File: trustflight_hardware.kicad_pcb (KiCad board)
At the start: 4 copper layers, 30.5 x 27 mm, 69 parts, among them J1 Conn_01x02, J10 Dronecode_Telemetry, J2 Conn_01x02, J3 Conn_01x02, J4 Conn_01x02, J5 Conn_01x01, J6 Conn_01x02, J7 Conn_01x02, J8 Conn_01x03, J9 swd-4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

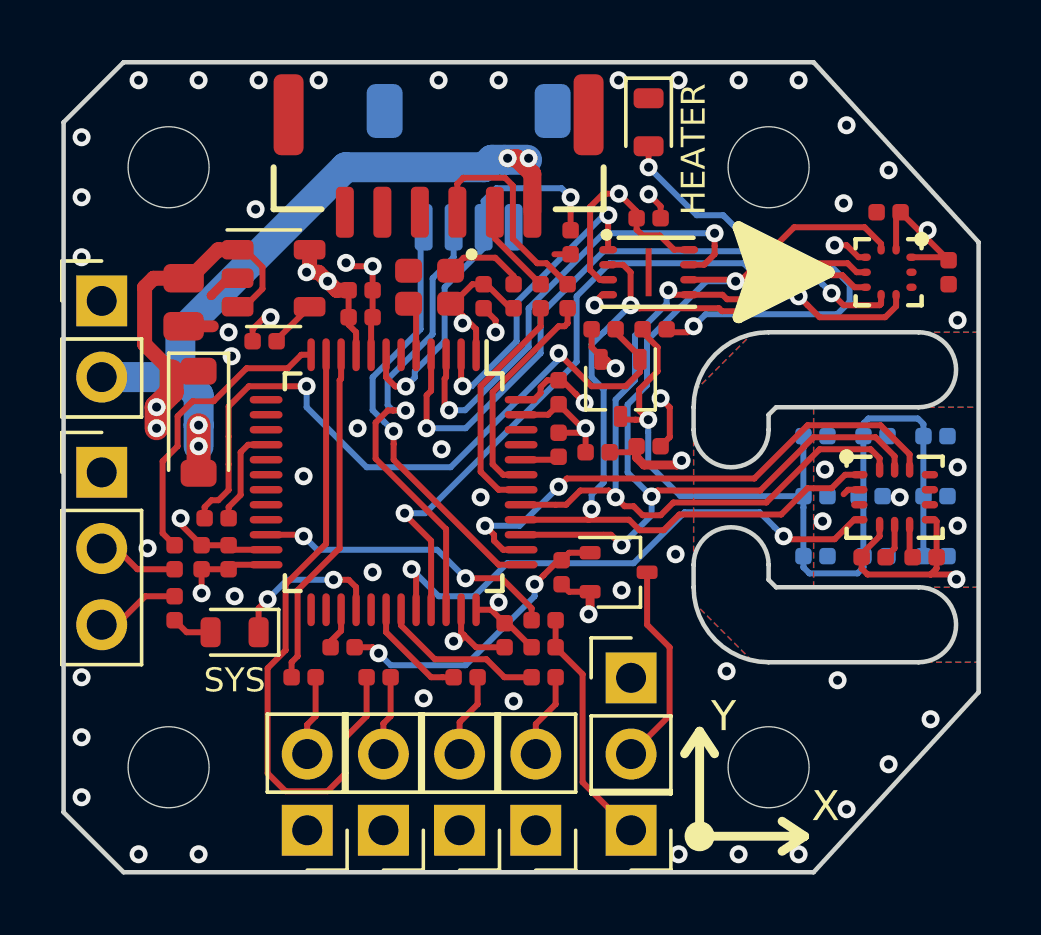
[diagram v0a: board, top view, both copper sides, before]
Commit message: Rev. B, fixed non 5V tolerant pins for heater/buzzer
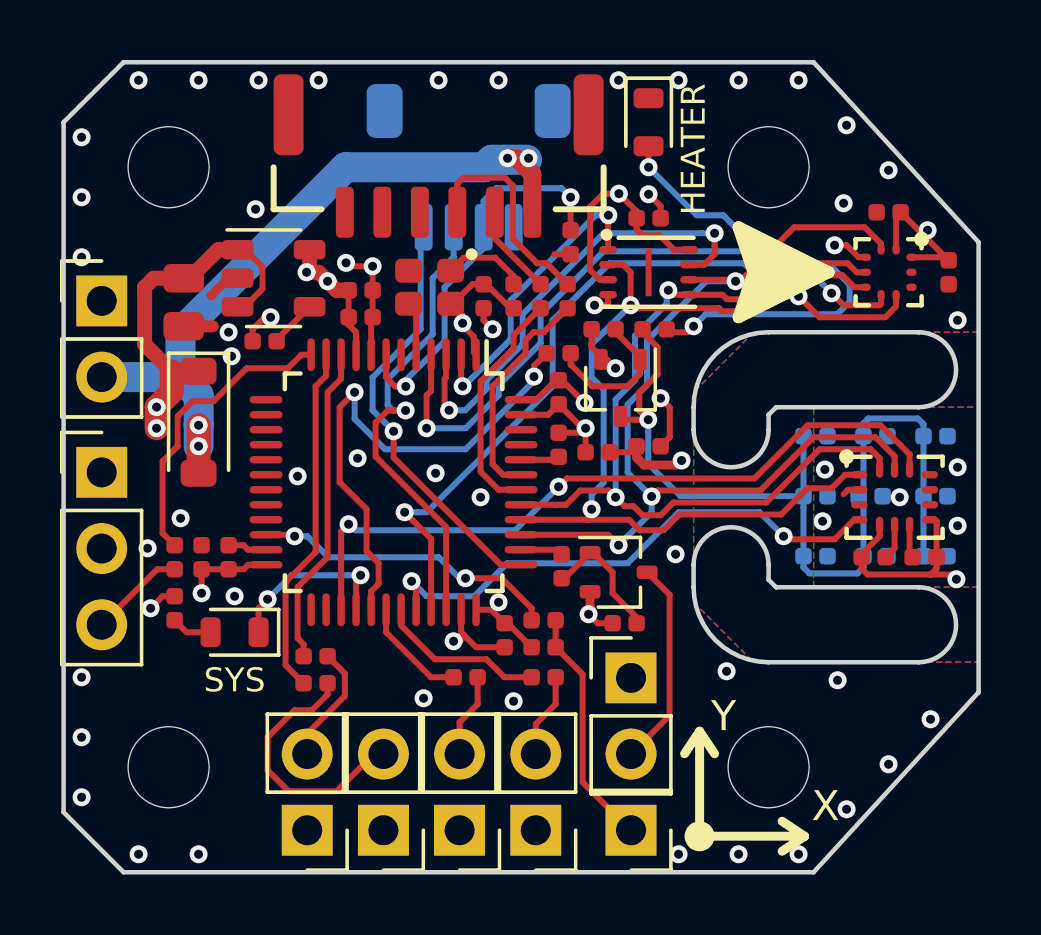
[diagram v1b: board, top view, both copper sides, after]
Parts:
- moved R1 12.7 mm to (143.0, 86.2), turned to 180 degrees
- moved R23 7.78 mm to (143.1, 93.3), turned to 90 degrees
- moved R20 2.70 mm to (145.2, 95.2), turned to 180 degrees
- moved R3 2.11 mm to (134.9, 97.2)
- moved R2 0.81 mm to (134.9, 96.3)
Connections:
- J8 pad 2: /F.port_P -> /VSYS
- J8 pad 3: /VSYS -> /F.port_P
- U4 pad 16: /HEATER -> (no net)
- U4 pad 27: /BUZZER -> /IMU_CS
- U4 pad 29: (no net) -> /HEATER
- U4 pad 38: /IMU_CS -> /BUZZER
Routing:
- net Net-(Q1-Pad1): track 23.7 -> 4.79 mm, vias 2 -> 0
- net /HEATER: track 3.32 -> 17.4 mm, vias 0 -> 2
- net /M2: track 21.3 -> 11.8 mm
- net /M2_P: track 2.66 -> 8.73 mm
- net /IMU_CS: track 18.1 -> 24.1 mm
- net Net-(Q2-Pad1): track 9.89 -> 4.35 mm, vias 2 -> 0
- net GND: track 32.3 -> 30.2 mm, vias 59 -> 57
- net /VSYS: track 80.7 -> 79.0 mm, vias 4 -> 5
- net /M1_P: track 2.68 -> 4.02 mm
- net /F.port_P: track 2.22 -> 3.22 mm
- net /M1: track 11.4 -> 10.7 mm
- net /LED: track 5.30 -> 5.87 mm
- net /IMU_INT: track 18.7 -> 18.1 mm

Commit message: Fixes for new KiCAD version and minor update to kicad_libs
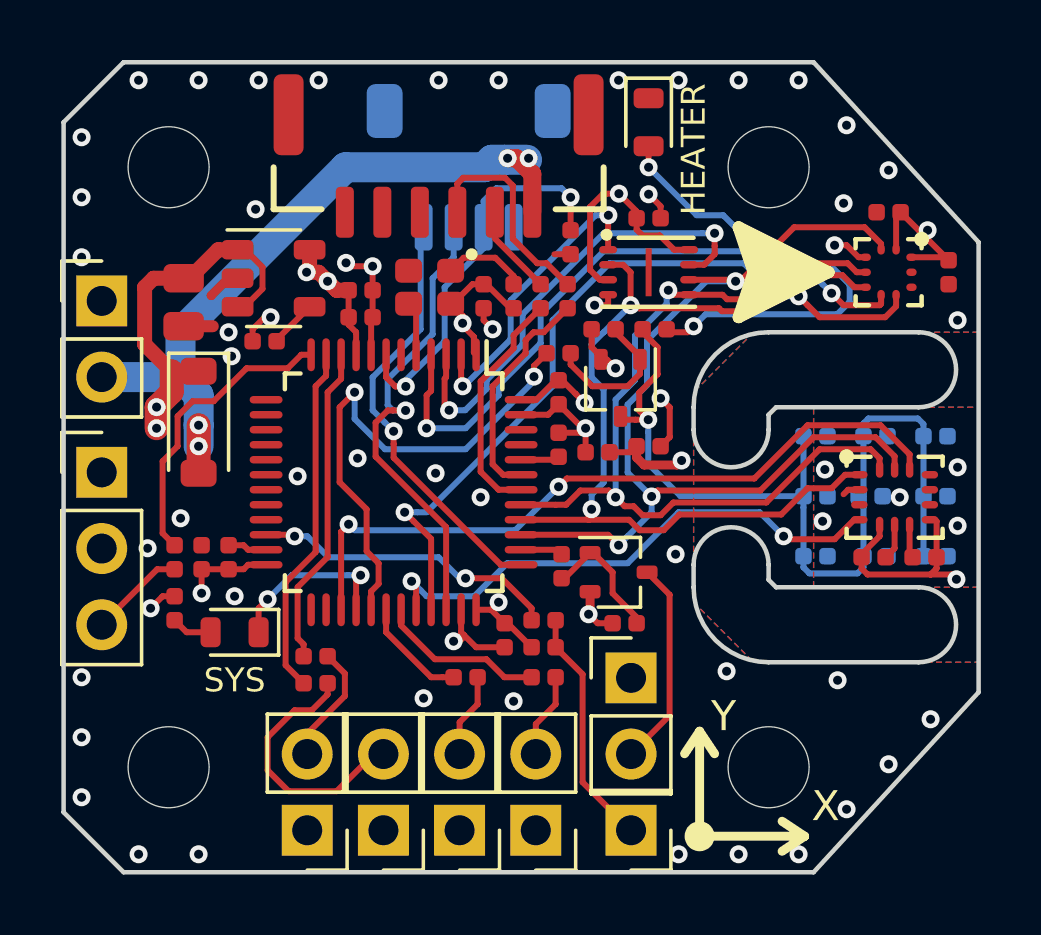
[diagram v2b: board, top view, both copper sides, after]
